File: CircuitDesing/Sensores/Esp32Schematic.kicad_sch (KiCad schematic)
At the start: 7 parts, among them SW1 SW_Push, SW2 SW_Push, U1 ESP32-WROOM-32

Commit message: Eliminado Actuadores
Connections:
- net +3.3V is gone; now on net 3.3v: R1.1
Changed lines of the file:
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@@
   (junction (at 101.6 52.07) (diameter 0) (color 0 0 0 0)
   )
+  (junction (at 80.01 48.26) (diameter 0) (color 0 0 0 0)
+  )
   (wire (pts (xy 92.71 53.34) (xy 101.6 53.34))
     (stroke (width 0) (type default) (color 0 0 0 0))
@@
     (stroke (width 0) (type default) (color 0 0 0 0))
   )
+  (wire (pts (xy 80.01 48.26) (xy 78.74 48.26))
+    (stroke (width 0) (type default) (color 0 0 0 0))
+  )
   (wire (pts (xy 63.5 78.74) (xy 62.23 80.01))
     (stroke (width 0) (type default) (color 0 0 0 0))
@@
     (stroke (width 0) (type default) (color 0 0 0 0))
   )
-  (wire (pts (xy 87.63 48.26) (xy 78.74 48.26))
+  (wire (pts (xy 87.63 48.26) (xy 80.01 48.26))
     (stroke (width 0) (type default) (color 0 0 0 0))
   )
   (wire (pts (xy 92.71 48.26) (xy 101.6 48.26))
+    (stroke (width 0) (type default) (color 0 0 0 0))
+  )
+  (wire (pts (xy 63.5 54.61) (xy 80.01 54.61))
+    (stroke (width 0) (type default) (color 0 0 0 0))
+  )
+  (wire (pts (xy 80.01 54.61) (xy 80.01 48.26))
     (stroke (width 0) (type default) (color 0 0 0 0))
   )
@@
     (pin "9")
   )
-  (symbol (lib_id "power:+3.3V") (at 63.5 54.61 0) (unit 1)
-    (in_bom yes) (on_board yes) (fields_autoplaced)
-    (property "Reference" "#PWR0102" (id 0) (at 63.5 58.42 0)
-      (effects (font (size 1.27 1.27)) hide)
-    )
-    (property "Value" "+3.3V" (id 1) (at 63.5 49.53 0))
-    (property "Footprint" "" (id 2) (at 63.5 54.61 0)
-      (effects (font (size 1.27 1.27)) hide)
-    )
-    (property "Datasheet" "" (id 3) (at 63.5 54.61 0)
-      (effects (font (size 1.27 1.27)) hide)
-    )
-    (pin "1")
-  )
   (symbol (lib_id "Switch:SW_Push") (at 121.92 68.58 0) (unit 1)

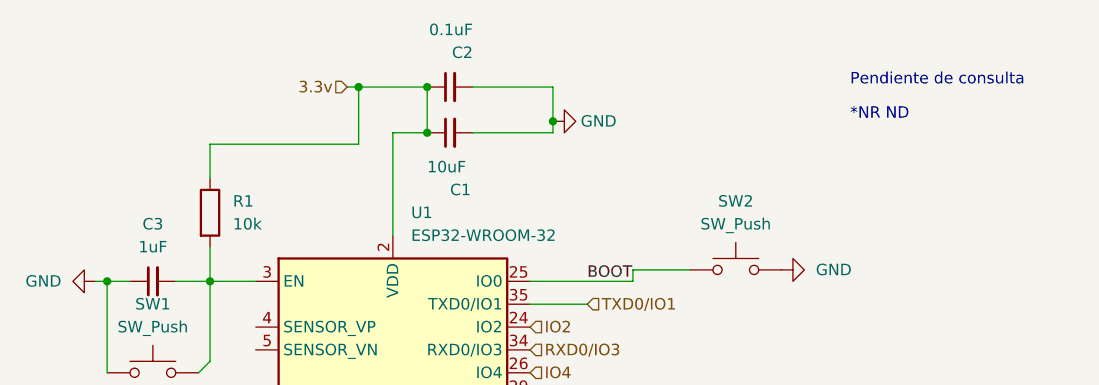
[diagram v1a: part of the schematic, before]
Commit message: Modificaciones generales
Modificaciones a esquemático,  interacción con otros grupos, sistema de potencia.
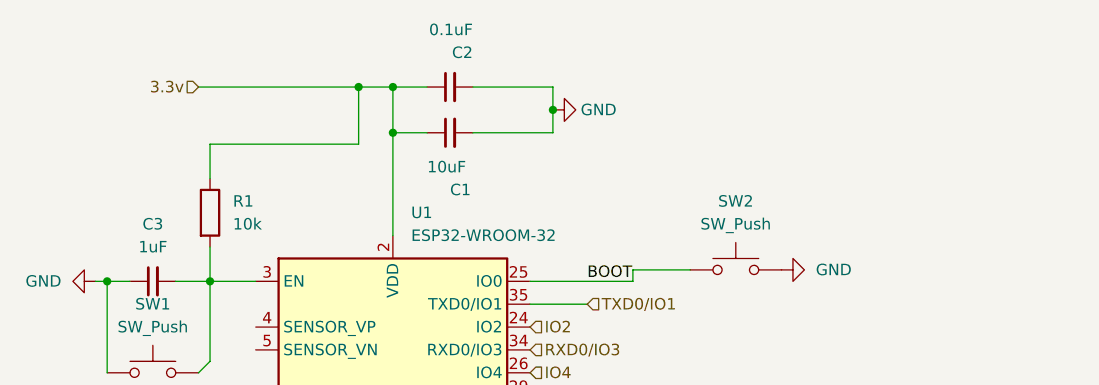
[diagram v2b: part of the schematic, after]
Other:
- note removed: "*NR ND"
- note removed: "Pendiente de consulta"
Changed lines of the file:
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@@
 (kicad_sch (version 20211123) (generator eeschema)
   (paper "A4")
-  (junction (at 87.63 48.26) (diameter 0) (color 0 0 0 0)
-  )
-  (junction (at 87.63 53.34) (diameter 0) (color 0 0 0 0)
+  (junction (at 83.82 48.26) (diameter 0) (color 0 0 0 0)
   )
   (junction (at 63.5 69.85) (diameter 0) (color 0 0 0 0)
@@
   (junction (at 52.07 69.85) (diameter 0) (color 0 0 0 0)
   )
-  (junction (at 101.6 52.07) (diameter 0) (color 0 0 0 0)
+  (junction (at 83.82 53.34) (diameter 0) (color 0 0 0 0)
+  )
+  (junction (at 101.6 50.8) (diameter 0) (color 0 0 0 0)
   )
   (junction (at 80.01 48.26) (diameter 0) (color 0 0 0 0)
@@
     (stroke (width 0) (type default) (color 0 0 0 0))
   )
+  (wire (pts (xy 62.23 48.26) (xy 80.01 48.26))
+    (stroke (width 0) (type default) (color 0 0 0 0))
+  )
   (wire (pts (xy 63.5 69.85) (xy 63.5 78.74))
     (stroke (width 0) (type default) (color 0 0 0 0))
@@
     (stroke (width 0) (type default) (color 0 0 0 0))
   )
-  (wire (pts (xy 80.01 48.26) (xy 78.74 48.26))
-    (stroke (width 0) (type default) (color 0 0 0 0))
-  )
   (wire (pts (xy 63.5 78.74) (xy 62.23 80.01))
     (stroke (width 0) (type default) (color 0 0 0 0))
   )
+  (wire (pts (xy 83.82 48.26) (xy 80.01 48.26))
+    (stroke (width 0) (type default) (color 0 0 0 0))
+  )
   (wire (pts (xy 59.69 69.85) (xy 63.5 69.85))
     (stroke (width 0) (type default) (color 0 0 0 0))
   )
-  (wire (pts (xy 87.63 53.34) (xy 87.63 48.26))
-    (stroke (width 0) (type default) (color 0 0 0 0))
-  )
   (wire (pts (xy 83.82 53.34) (xy 87.63 53.34))
     (stroke (width 0) (type default) (color 0 0 0 0))
   )
+  (wire (pts (xy 83.82 48.26) (xy 83.82 53.34))
+    (stroke (width 0) (type default) (color 0 0 0 0))
+  )
   (wire (pts (xy 52.07 69.85) (xy 54.61 69.85))
     (stroke (width 0) (type default) (color 0 0 0 0))
@@
     (stroke (width 0) (type default) (color 0 0 0 0))
   )
-  (wire (pts (xy 87.63 48.26) (xy 80.01 48.26))
+  (wire (pts (xy 87.63 48.26) (xy 83.82 48.26))
     (stroke (width 0) (type default) (color 0 0 0 0))
   )
@@
     (stroke (width 0) (type default) (color 0 0 0 0))
   )
-  (wire (pts (xy 101.6 53.34) (xy 101.6 52.07))
+  (wire (pts (xy 101.6 53.34) (xy 101.6 50.8))
     (stroke (width 0) (type default) (color 0 0 0 0))
   )
@@
     (stroke (width 0) (type default) (color 0 0 0 0))
   )
-  (wire (pts (xy 101.6 48.26) (xy 101.6 52.07))
+  (wire (pts (xy 101.6 48.26) (xy 101.6 50.8))
     (stroke (width 0) (type default) (color 0 0 0 0))
   )
@@
   (wire (pts (xy 99.06 69.85) (xy 110.49 69.85))
     (stroke (width 0) (type default) (color 0 0 0 0))
-  )
-  (text "Pendiente de consulta" (at 134.62 48.26 0)
-    (effects (font (size 1.27 1.27)) (justify left bottom))
-  )
-  (text "*NR ND" (at 134.62 52.07 0)
-    (effects (font (size 1.27 1.27)) (justify left bottom))
   )
   (label "BOOT" (at 105.41 69.85 0)
@@
     (effects (font (size 1.27 1.27)) (justify left))
   )
-  (hierarchical_label "3.3v" (shape input) (at 78.74 48.26 180)
+  (hierarchical_label "3.3v" (shape input) (at 62.23 48.26 180)
     (effects (font (size 1.27 1.27)) (justify right))
   )
@@
     (pin "2")
   )
-  (symbol (lib_id "power:GND") (at 101.6 52.07 90) (unit 1)
+  (symbol (lib_id "power:GND") (at 101.6 50.8 90) (unit 1)
     (in_bom yes) (on_board yes)
-    (property "Reference" "#PWR0105" (id 0) (at 107.95 52.07 0)
-      (effects (font (size 1.27 1.27)) hide)
-    )
-    (property "Value" "GND" (id 1) (at 106.68 52.07 90))
-    (property "Footprint" "" (id 2) (at 101.6 52.07 0)
-      (effects (font (size 1.27 1.27)) hide)
-    )
-    (property "Datasheet" "" (id 3) (at 101.6 52.07 0)
-      (effects (font (size 1.27 1.27)) hide)
-    )
+    (property "Reference" "#PWR0105" (id 0) (at 107.95 50.8 0)
+      (effects (font (size 1.27 1.27)) hide)
+    )
+    (property "Value" "GND" (id 1) (at 106.68 50.8 90))
+    (property "Footprint" "" (id 2) (at 101.6 50.8 0)
+      (effects (font (size 1.27 1.27)) hide)
+    )
+    (property "Datasheet" "" (id 3) (at 101.6 50.8 0)
+      (effects (font (size 1.27 1.27)) hide)
+    )

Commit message: Huellas
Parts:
- added C4: 1uF, Capacitor_SMD:C_0603_1608Metric_Pad1.08x0.95mm_HandSolder, symbol Device:C_Small
- added R3: 10k, Resistor_SMD:R_0603_1608Metric_Pad0.98x0.95mm_HandSolder, symbol Device:R
- SW1, SW2: footprint (none) -> Button_Switch_SMD:SW_Push_1P1T_NO_6x6mm_H9.5mm
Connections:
- net BOOT: now also C4.1, R3.2
- net GND: now also C4.2, R3.1
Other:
- moved on the sheet: SW2
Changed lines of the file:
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@@
 (kicad_sch (version 20211123) (generator eeschema)
   (paper "A4")
+  (junction (at 105.41 69.85) (diameter 0) (color 0 0 0 0)
+  )
   (junction (at 83.82 48.26) (diameter 0) (color 0 0 0 0)
   )
@@
   (junction (at 52.07 69.85) (diameter 0) (color 0 0 0 0)
   )
+  (junction (at 101.6 53.34) (diameter 0) (color 0 0 0 0)
+  )
   (junction (at 83.82 53.34) (diameter 0) (color 0 0 0 0)
   )
+  (junction (at 130.81 68.58) (diameter 0) (color 0 0 0 0)
+  )
   (junction (at 101.6 50.8) (diameter 0) (color 0 0 0 0)
   )
+  (junction (at 119.38 68.58) (diameter 0) (color 0 0 0 0)
+  )
   (junction (at 80.01 48.26) (diameter 0) (color 0 0 0 0)
   )
@@
     (stroke (width 0) (type default) (color 0 0 0 0))
   )
+  (wire (pts (xy 119.38 77.47) (xy 123.19 77.47))
+    (stroke (width 0) (type default) (color 0 0 0 0))
+  )
+  (wire (pts (xy 105.41 63.5) (xy 105.41 69.85))
+    (stroke (width 0) (type default) (color 0 0 0 0))
+  )
   (wire (pts (xy 62.23 48.26) (xy 80.01 48.26))
     (stroke (width 0) (type default) (color 0 0 0 0))
@@
     (stroke (width 0) (type default) (color 0 0 0 0))
   )
+  (wire (pts (xy 128.27 77.47) (xy 130.81 77.47))
+    (stroke (width 0) (type default) (color 0 0 0 0))
+  )
+  (wire (pts (xy 133.35 68.58) (xy 130.81 68.58))
+    (stroke (width 0) (type default) (color 0 0 0 0))
+  )
   (wire (pts (xy 63.5 78.74) (xy 62.23 80.01))
     (stroke (width 0) (type default) (color 0 0 0 0))
   )
+  (wire (pts (xy 101.6 55.88) (xy 101.6 53.34))
+    (stroke (width 0) (type default) (color 0 0 0 0))
+  )
+  (wire (pts (xy 105.41 69.85) (xy 110.49 69.85))
+    (stroke (width 0) (type default) (color 0 0 0 0))
+  )
   (wire (pts (xy 83.82 48.26) (xy 80.01 48.26))
     (stroke (width 0) (type default) (color 0 0 0 0))
@@
     (stroke (width 0) (type default) (color 0 0 0 0))
   )
-  (wire (pts (xy 116.84 68.58) (xy 110.49 68.58))
+  (wire (pts (xy 110.49 68.58) (xy 119.38 68.58))
+    (stroke (width 0) (type default) (color 0 0 0 0))
+  )
+  (wire (pts (xy 130.81 77.47) (xy 130.81 68.58))
     (stroke (width 0) (type default) (color 0 0 0 0))
   )
@@
     (stroke (width 0) (type default) (color 0 0 0 0))
   )
+  (wire (pts (xy 119.38 77.47) (xy 119.38 68.58))
+    (stroke (width 0) (type default) (color 0 0 0 0))
+  )
+  (wire (pts (xy 119.38 68.58) (xy 120.65 68.58))
+    (stroke (width 0) (type default) (color 0 0 0 0))
+  )
   (wire (pts (xy 50.8 69.85) (xy 52.07 69.85))
     (stroke (width 0) (type default) (color 0 0 0 0))
@@
     (stroke (width 0) (type default) (color 0 0 0 0))
   )
+  (wire (pts (xy 107.95 55.88) (xy 101.6 55.88))
+    (stroke (width 0) (type default) (color 0 0 0 0))
+  )
   (wire (pts (xy 80.01 54.61) (xy 80.01 48.26))
     (stroke (width 0) (type default) (color 0 0 0 0))
@@
     (stroke (width 0) (type default) (color 0 0 0 0))
   )
+  (wire (pts (xy 107.95 63.5) (xy 105.41 63.5))
+    (stroke (width 0) (type default) (color 0 0 0 0))
+  )
   (wire (pts (xy 83.82 137.16) (xy 83.82 135.89))
     (stroke (width 0) (type default) (color 0 0 0 0))
   )
-  (wire (pts (xy 99.06 69.85) (xy 110.49 69.85))
+  (wire (pts (xy 99.06 69.85) (xy 105.41 69.85))
     (stroke (width 0) (type default) (color 0 0 0 0))
   )
@@
   (symbol (lib_id "power:GND") (at 50.8 69.85 270) (unit 1)
     (in_bom yes) (on_board yes) (fields_autoplaced)
-    (property "Reference" "#PWR?" (id 0) (at 44.45 69.85 0)
+    (property "Reference" "#PWR0101" (id 0) (at 44.45 69.85 0)
       (effects (font (size 1.27 1.27)) hide)
     )
@@
     )
     (pin "1")
+  )
+  (symbol (lib_id "Device:C_Small") (at 125.73 77.47 90) (unit 1)
+    (in_bom yes) (on_board yes) (fields_autoplaced)
+    (property "Reference" "C4" (id 0) (at 125.7363 71.12 90))
+    (property "Value" "1uF" (id 1) (at 125.7363 73.66 90))
+    (property "Footprint" "Capacitor_SMD:C_0603_1608Metric_Pad1.08x0.95mm_HandSolder" (id 2) (at 125.73 77.47 0)
+      (effects (font (size 1.27 1.27)) hide)
+    )
+    (property "Datasheet" "~" (id 3) (at 125.73 77.47 0)
+      (effects (font (size 1.27 1.27)) hide)
+    )
+    (pin "1")
+    (pin "2")
   )
   (symbol (lib_id "Device:C_Small") (at 90.17 48.26 90) (unit 1)
@@
     (pin "9")
   )
-  (symbol (lib_id "Switch:SW_Push") (at 121.92 68.58 0) (unit 1)
-    (in_bom yes) (on_board yes) (fields_autoplaced)
-    (property "Reference" "SW2" (id 0) (at 121.92 60.96 0))
-    (property "Value" "SW_Push" (id 1) (at 121.92 63.5 0))
-    (property "Footprint" "" (id 2) (at 121.92 63.5 0)
-      (effects (font (size 1.27 1.27)) hide)
-    )
-    (property "Datasheet" "~" (id 3) (at 121.92 63.5 0)
-      (effects (font (size 1.27 1.27)) hide)
-    )
-    (pin "1")
-    (pin "2")
-  )
-  (symbol (lib_id "power:GND") (at 127 68.58 90) (unit 1)
-    (in_bom yes) (on_board yes) (fields_autoplaced)
-    (property "Reference" "#PWR?" (id 0) (at 133.35 68.58 0)
-      (effects (font (size 1.27 1.27)) hide)
-    )
-    (property "Value" "GND" (id 1) (at 130.81 68.5799 90)
+  (symbol (lib_id "Device:R") (at 107.95 59.69 0) (unit 1)
+    (in_bom yes) (on_board yes) (fields_autoplaced)
+    (property "Reference" "R3" (id 0) (at 110.49 58.4199 0)
+      (effects (font (size 1.27 1.27)) (justify left))
+    )
+    (property "Value" "10k" (id 1) (at 110.49 60.9599 0)
+      (effects (font (size 1.27 1.27)) (justify left))
+    )
+    (property "Footprint" "Resistor_SMD:R_0603_1608Metric_Pad0.98x0.95mm_HandSolder" (id 2) (at 106.172 59.69 90)
+      (effects (font (size 1.27 1.27)) hide)
+    )
+    (property "Datasheet" "~" (id 3) (at 107.95 59.69 0)
+      (effects (font (size 1.27 1.27)) hide)
+    )
+    (pin "1")
+    (pin "2")
+  )
+  (symbol (lib_id "Switch:SW_Push") (at 125.73 68.58 0) (unit 1)
+    (in_bom yes) (on_board yes) (fields_autoplaced)
+    (property "Reference" "SW2" (id 0) (at 125.73 60.96 0))
+    (property "Value" "SW_Push" (id 1) (at 125.73 63.5 0))
+    (property "Footprint" "Button_Switch_SMD:SW_Push_1P1T_NO_6x6mm_H9.5mm" (id 2) (at 125.73 63.5 0)
+      (effects (font (size 1.27 1.27)) hide)
+    )
+    (property "Datasheet" "~" (id 3) (at 125.73 63.5 0)
+      (effects (font (size 1.27 1.27)) hide)
+    )
+    (pin "1")
+    (pin "2")
+  )
+  (symbol (lib_id "power:GND") (at 133.35 68.58 90) (unit 1)
+    (in_bom yes) (on_board yes) (fields_autoplaced)
+    (property "Reference" "#PWR0102" (id 0) (at 139.7 68.58 0)
+      (effects (font (size 1.27 1.27)) hide)
+    )
+    (property "Value" "GND" (id 1) (at 137.16 68.5799 90)
       (effects (font (size 1.27 1.27)) (justify right))
     )
-    (property "Footprint" "" (id 2) (at 127 68.58 0)
-      (effects (font (size 1.27 1.27)) hide)
-    )
-    (property "Datasheet" "" (id 3) (at 127 68.58 0)
+    (property "Footprint" "" (id 2) (at 133.35 68.58 0)
+      (effects (font (size 1.27 1.27)) hide)
+    )
+    (property "Datasheet" "" (id 3) (at 133.35 68.58 0)
       (effects (font (size 1.27 1.27)) hide)
     )
@@
     (property "Reference" "SW1" (id 0) (at 57.15 72.39 0))
     (property "Value" "SW_Push" (id 1) (at 57.15 74.93 0))
-    (property "Footprint" "" (id 2) (at 57.15 74.93 0)
-      (effects (font (size 1.27 1.27)) hide)
-    )
+    (property "Footprint" "Button_Switch_SMD:SW_Push_1P1T_NO_6x6mm_H9.5mm" (id 2) (at 57.15 74.93 0)
+      (effects (font (size 1.27 1.27)) hide)
+    )
